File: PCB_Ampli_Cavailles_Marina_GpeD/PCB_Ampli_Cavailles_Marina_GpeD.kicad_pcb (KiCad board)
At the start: 2 copper layers, 52 parts, among them J2 Conn_01x02, J3 Conn_01x03, Q1 2N2907, Q10 TIP32, Q11 BD138, Q12 TIP31, Q13 2N2222, Q2 2N2907, Q3 2N2907, Q4 2N2222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

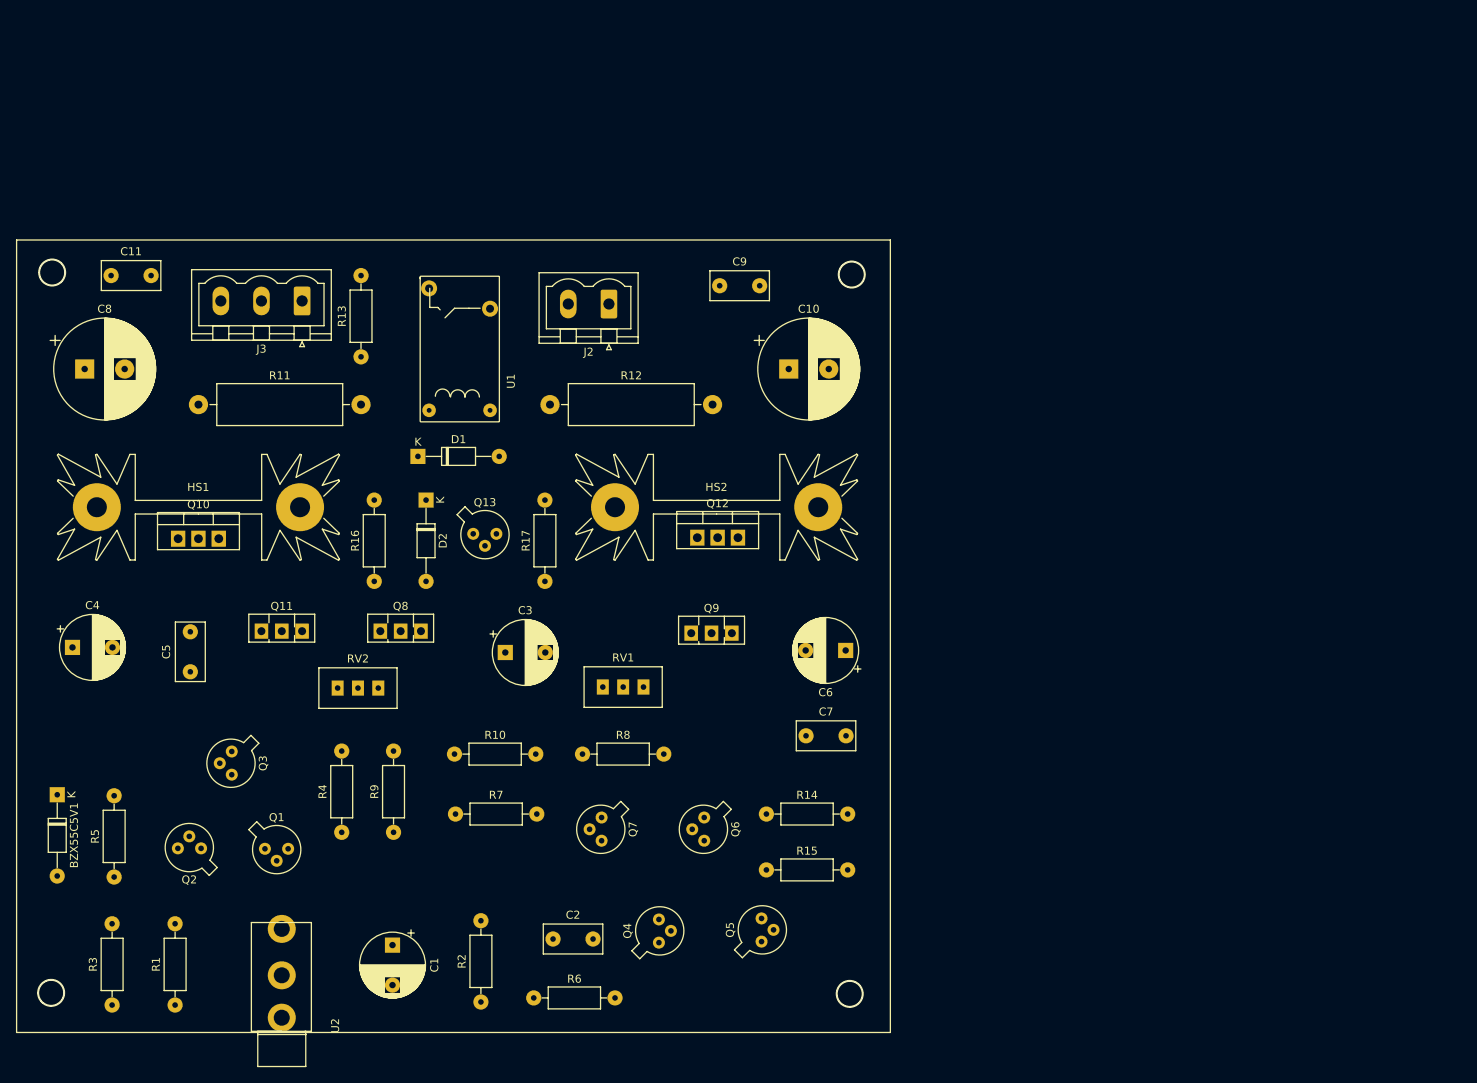
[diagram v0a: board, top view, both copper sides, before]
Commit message: Il manque finir le routage
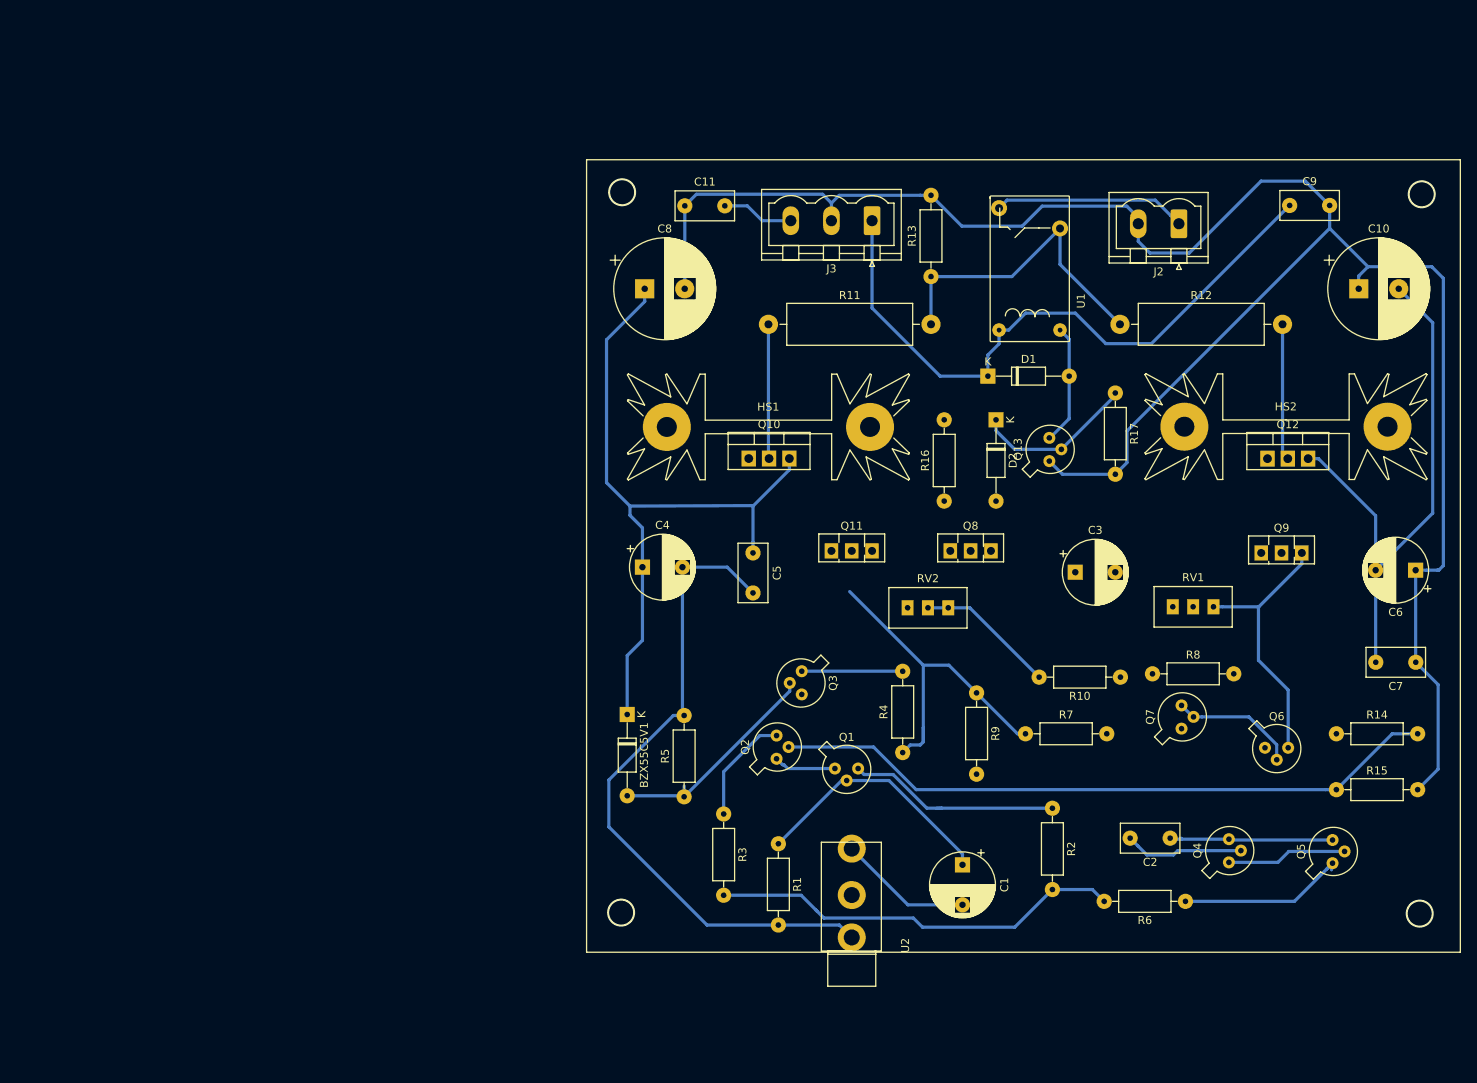
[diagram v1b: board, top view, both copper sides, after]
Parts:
- moved R10 83.8 mm to (163.4, 108.0), turned to 180 degrees
- moved R6 82.4 mm to (171.5, 136.0), turned to 180 degrees
- moved R3 80.1 mm to (113.8, 125.1), turned to 270 degrees
- moved C2 78.2 mm to (169.6, 128.1), turned to 180 degrees
- moved R1 78.1 mm to (120.6, 128.8), turned to 270 degrees
- moved C7 76.8 mm to (200.3, 106.1), turned to 180 degrees
- moved R2 75.4 mm to (154.9, 124.4), turned to 270 degrees
- moved R17 75.1 mm to (162.7, 72.5), turned to 270 degrees
- moved R9 74.9 mm to (145.4, 110.0), turned to 270 degrees
- moved Q7 73.6 mm to (171.1, 114.2), turned to 90 degrees
- moved Q2 73.1 mm to (120.5, 118.0), turned to 90 degrees
- moved Q13 72.5 mm to (154.6, 80.8), turned to 90 degrees
- moved C11 72.2 mm to (108.9, 49.1)
- moved Q5 72.0 mm to (190.0, 131.0)
- moved Q10 72.0 mm to (116.9, 80.7)
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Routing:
- net GND: track 0.00 -> 333.0 mm
- net +12V: track 0.00 -> 211.9 mm
- net -12V: track 0.00 -> 130.6 mm
- net Net-(Q2-Pad2): track 0.00 -> 83.7 mm
- net Net-(C2-Pad2): track 0.00 -> 41.9 mm
- net Net-(R11-Pad2): track 0.00 -> 39.7 mm
- net Net-(Q6-Pad3): track 0.00 -> 33.8 mm
- net Net-(C1-Pad1): track 0.00 -> 31.4 mm
- net Net-(BZX55C5V1-Pad2): track 0.00 -> 28.2 mm
- net Net-(J2-Pad1): track 0.00 -> 24.1 mm
- net Net-(Q5-Pad1): track 0.00 -> 22.5 mm
- net Net-(C2-Pad1): track 0.00 -> 20.5 mm
- net Net-(D2-Pad1): track 0.00 -> 20.3 mm
- net Net-(R10-Pad2): track 0.00 -> 17.5 mm
- net Net-(Q11-Pad1): track 0.00 -> 17.1 mm
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
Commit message: Il manque 1 routage
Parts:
- moved Q11 57.0 mm to (184.2, 90.4), turned to 180 degrees
- moved Q9 42.2 mm to (138.8, 92.2)
- moved R14 13.2 mm to (203.5, 116.5), turned to 180 degrees
- moved Q8 9.75 mm to (151.6, 94.5), turned to 270 degrees
- moved C5 3.84 mm to (120.9, 94.2), turned to 180 degrees
- moved RV1 2.36 mm to (174.0, 97.1), turned to 90 degrees
- moved R9 1.83 mm to (145.5, 108.1)
- moved R7 0.63 mm to (151.6, 114.4)
- moved R4 0.43 mm to (135.7, 117.4)
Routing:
- net -12V: track 130.6 -> 478.9 mm
- net Net-(C2-Pad1): track 20.5 -> 239.3 mm
- net +12V: track 211.9 -> 407.4 mm
- net GND: track 333.0 -> 441.2 mm
- net Net-(Q1-Pad1): track 7.88 -> 105.4 mm
- net Net-(Q6-Pad1): track 0.00 -> 70.4 mm
- net Net-(Q10-Pad1): track 0.00 -> 66.3 mm
- net Net-(Q6-Pad3): track 33.8 -> 65.9 mm
- net Net-(C3-Pad1): track 0.00 -> 27.2 mm
- net Net-(Q7-Pad1): track 0.00 -> 27.1 mm
- net Net-(Q10-Pad2): track 16.9 -> 43.7 mm
- net Net-(Q8-Pad3): track 0.00 -> 22.4 mm
- net Net-(Q2-Pad2): track 83.7 -> 70.7 mm
- net Net-(C2-Pad2): track 41.9 -> 52.5 mm
- net Net-(Q6-Pad2): track 15.8 -> 25.7 mm
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
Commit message: Routage fini
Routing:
- net Net-(R11-Pad2): track 39.7 -> 266.8 mm
- net -12V: track 478.9 -> 468.5 mm
- net Net-(Q2-Pad2): track 70.7 -> 77.5 mm
- net GND: track 441.2 -> 445.4 mm
- net Net-(BZX55C5V1-Pad2): track 28.2 -> 26.7 mm
- net Net-(Q5-Pad1): track 22.5 -> 21.4 mm

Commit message: Changes
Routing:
- net +12V: track 407.4 -> 402.4 mm
- net Net-(Q6-Pad3): track 65.9 -> 67.4 mm
- net -12V: track 468.5 -> 469.0 mm

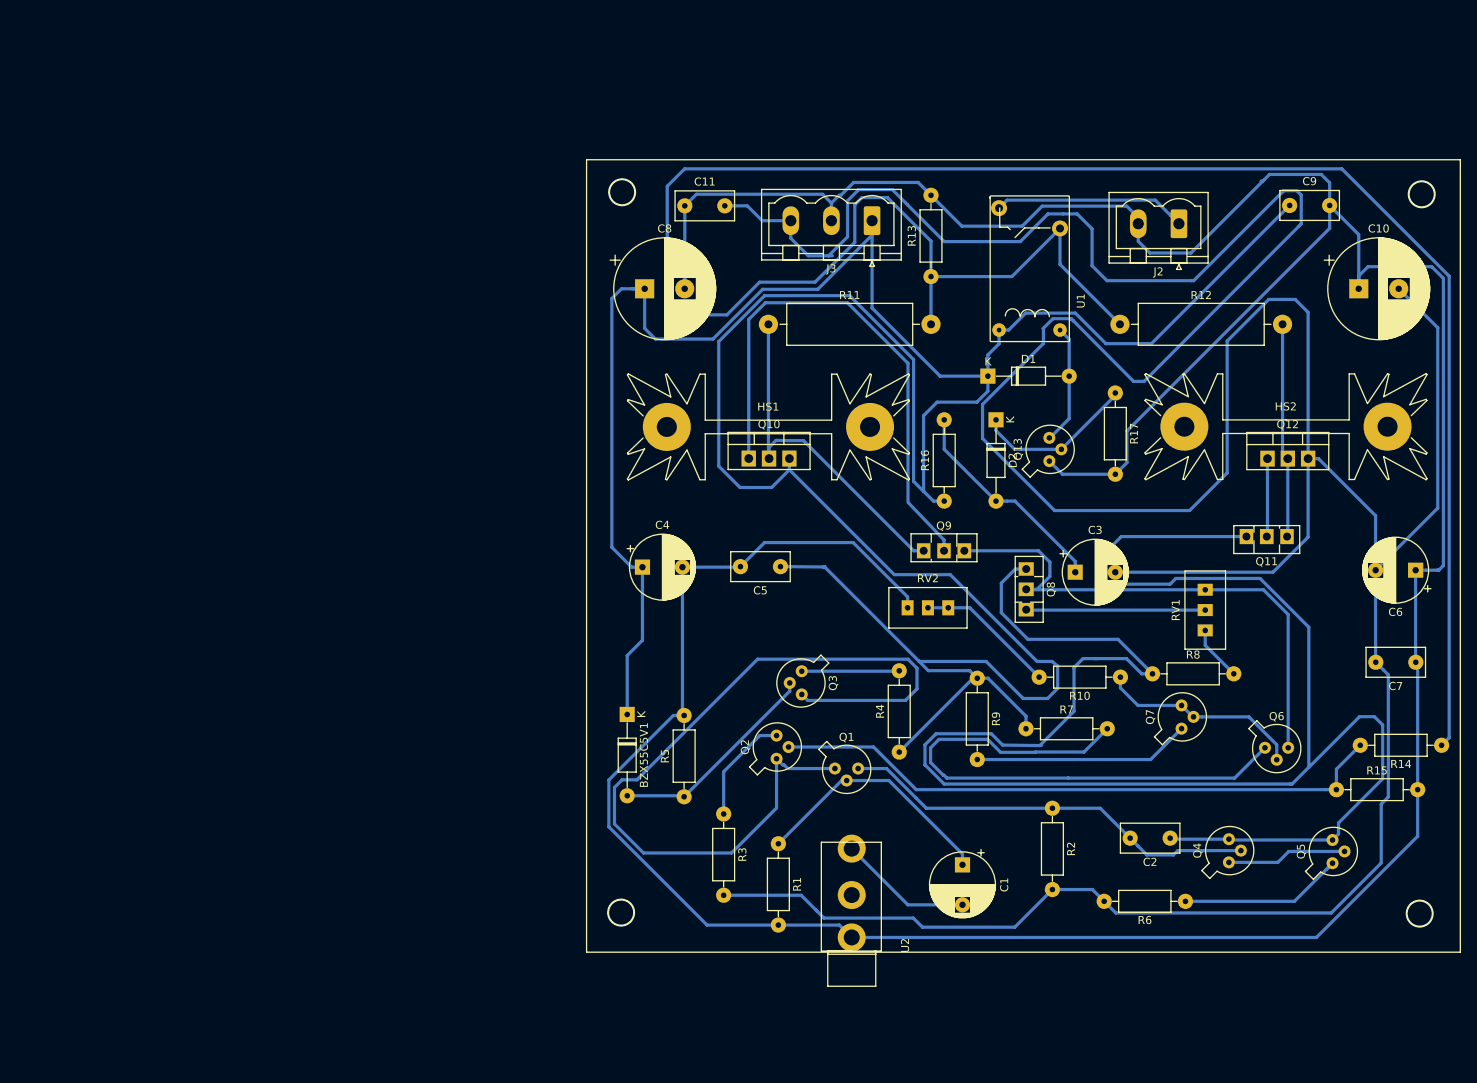
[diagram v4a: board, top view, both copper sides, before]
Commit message: New PCB
On a separé les sections: puissance et diff, et on a mis en place differents Track Witdh
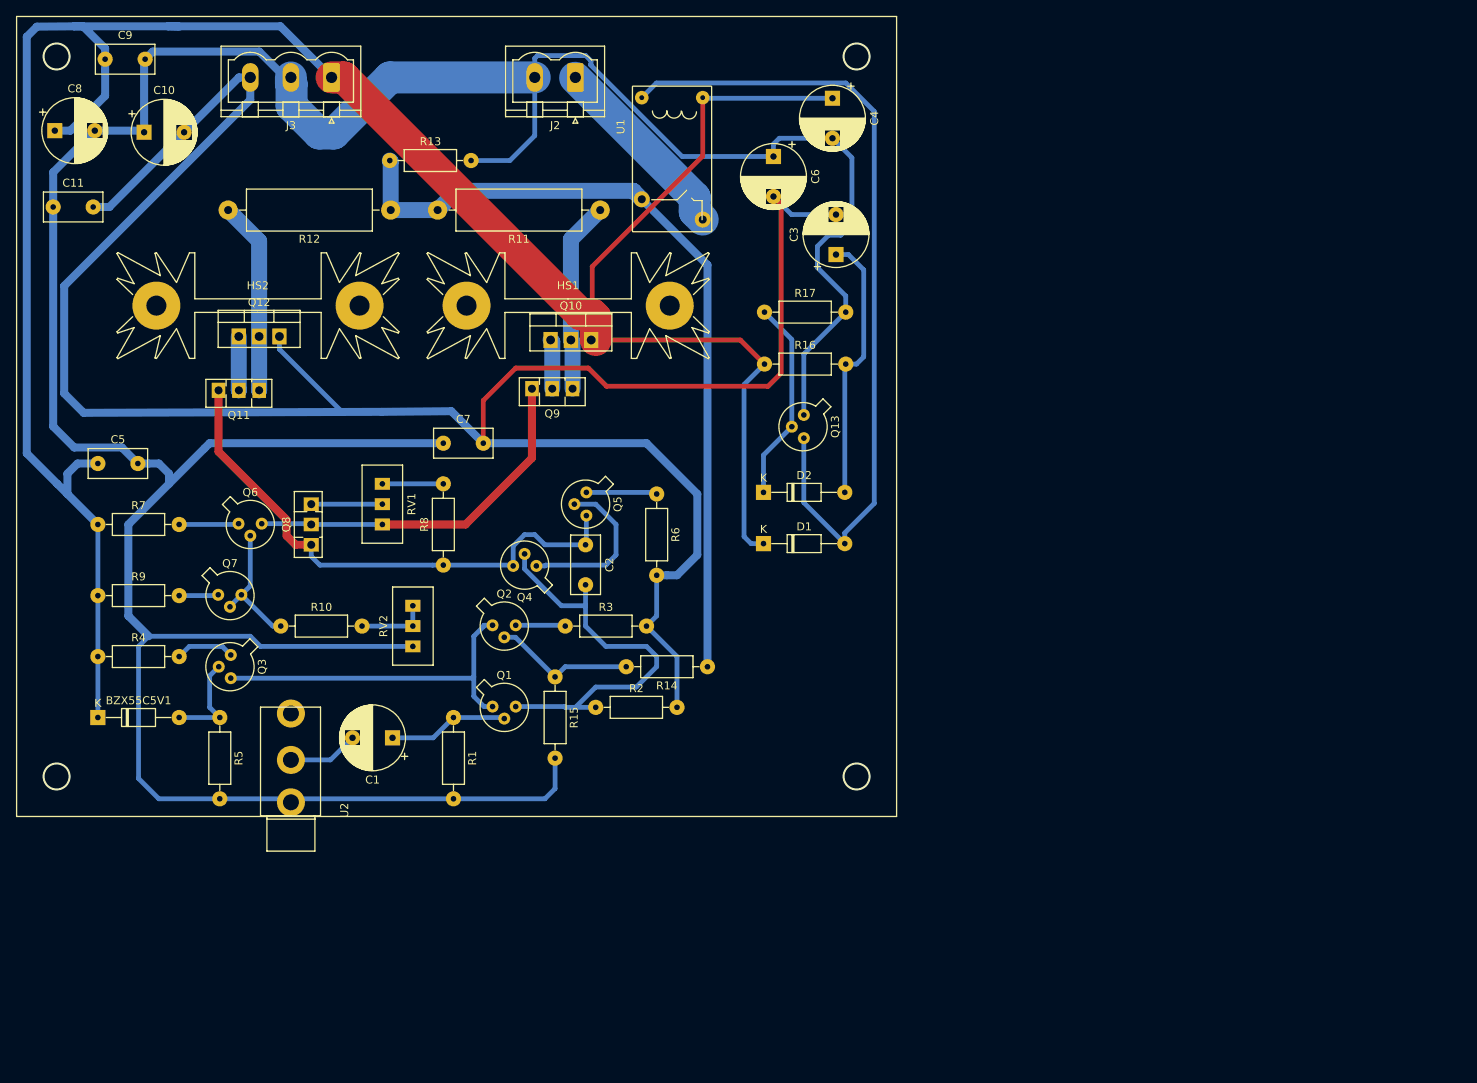
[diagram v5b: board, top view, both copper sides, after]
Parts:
- C1, C3: value 47u -> CP
- C10, C8: value 470u -> CP; footprint CmpAmpliAudioTR:CP_Radial_D12.5mm_P5.00mm -> CmpAmpliAudio:CP_Radial_D8.0mm_P5.00mm
- C11, C5, C7, C9: value 100n -> C
- C4, C6: value 10u -> CP
- moved C10 153.1 mm to (41.3, 39.9)
- moved C9 149.2 mm to (36.5, 30.7)
- moved Q6 131.3 mm to (53.3, 88.9)
- moved Q11 129.8 mm to (55.7, 72.1)
- moved Q12 129.5 mm to (53.2, 65.4)
- moved HS2 129.4 mm to (55.6, 61.5)
- moved C7 124.6 mm to (78.7, 78.7), turned to 0 degrees
- moved Q7 121.4 mm to (50.8, 97.8), turned to 0 degrees
- moved R7 118.8 mm to (35.6, 88.9)
- moved R9 110.4 mm to (35.6, 97.8), turned to 0 degrees
- moved U1 106.6 mm to (94.0, 10.5), turned to 270 degrees
- moved R10 105.2 mm to (58.4, 101.6), turned to 0 degrees
- moved Q5 104.2 mm to (96.5, 85.1), turned to 270 degrees
- moved RV1 103.2 mm to (71.1, 88.9), turned to 270 degrees
- moved R4 100.9 mm to (35.6, 105.4), turned to 0 degrees
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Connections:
- U2 pad T: Net-(U2-PadT) -> Net-(C1-Pad2)
- U2 pad TN: Net-(C1-Pad2) -> Net-(U2-PadTN)
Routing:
- net -12V: track 469.0 -> 287.8 mm
- net Net-(C2-Pad1): track 238.9 -> 68.8 mm
- net Net-(R11-Pad2): track 266.8 -> 101.1 mm
- net +12V: track 402.4 -> 303.0 mm
- net Net-(D1-Pad2): track 15.0 -> 102.1 mm
- net Net-(Q6-Pad1): track 70.4 -> 7.46 mm
- net Net-(Q1-Pad1): track 105.4 -> 43.8 mm
- net Net-(Q10-Pad1): track 66.4 -> 6.18 mm
- net Net-(Q2-Pad2): track 77.5 -> 17.8 mm
- net GND: track 445.4 -> 405.4 mm
- net Net-(Q7-Pad1): track 27.1 -> 4.92 mm
- net Net-(Q6-Pad3): track 67.4 -> 46.3 mm
- net Net-(Q10-Pad2): track 43.7 -> 23.9 mm
- net Net-(C1-Pad1): track 31.4 -> 15.1 mm
- net Net-(BZX55C5V1-Pad2): track 26.7 -> 12.4 mm
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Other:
- net class Default: clearance 0.3 -> 0.2
- net class FeCl3 added: clearance 0.2, trace_width 0.4, via_dia 0.8, via_drill 0.6
- net class PCB_GEI removed
- rule pad_to_mask_clearance: 0 -> 0.051
- rule trace_clearance: 0.3 -> 0.2
- rule via_min_size: 0.6 -> 0.4
- board text added: "DIFF EC"
- board text added: "Puissance"

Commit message: 4mm pour R13 à GND
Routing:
- net GND: track 405.4 -> 402.5 mm
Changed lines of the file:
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@@
     (thickness 1.6)
     (drawings 27)
-    (tracks 284)
+    (tracks 283)
     (zones 0)
     (modules 52)
@@
   )
   (setup
-    (last_trace_width 2)
+    (last_trace_width 4)
     (user_trace_width 0.6)
     (user_trace_width 1)
@@
   (segment (start 120.7421 40.62096) (end 120.00992 41.35314) (width 0.6) (layer B.Cu) (net 9))
   (segment (start 127.381 40.62096) (end 120.7421 40.62096) (width 0.6) (layer B.Cu) (net 9))
-  (segment (start 82.20456 43.40606) (end 87.06358 43.40606) (width 0.6) (layer B.Cu) (net 9))
-  (segment (start 90.17 40.29964) (end 90.17 33.02) (width 0.6) (layer B.Cu) (net 9))
-  (segment (start 87.06358 43.40606) (end 90.17 40.29964) (width 0.6) (layer B.Cu) (net 9))
   (segment (start 129.81686 43.05682) (end 127.381 40.62096) (width 0.6) (layer B.Cu) (net 9))
   (segment (start 129.81686 51.34102) (end 129.81686 43.05682) (width 0.6) (layer B.Cu) (net 9))
@@
   (segment (start 90.5005 30.2895) (end 90.17 30.62) (width 0.6) (layer B.Cu) (net 9))
   (segment (start 96.53778 30.2895) (end 90.5005 30.2895) (width 0.6) (layer B.Cu) (net 9))
+  (segment (start 90.17 35.44062) (end 82.20456 43.40606) (width 4) (layer B.Cu) (net 9))
+  (segment (start 90.17 33.02) (end 90.17 35.44062) (width 4) (layer B.Cu) (net 9))
   (segment (start 128.92278 89.949178) (end 132.60832 86.263638) (width 0.6) (layer B.Cu) (net 10))
   (segment (start 128.92278 91.29268) (end 128.92278 89.949178) (width 0.6) (layer B.Cu) (net 10))
